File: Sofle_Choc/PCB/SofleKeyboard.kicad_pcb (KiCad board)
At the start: 2 copper layers, 143.4 x 111.8 mm, 84 parts, among them J2 4PIN, J3 OLED, P1 i2c_pin, P2 i2c_pin, SW1 SW_PUSH_LED, SW10 SW_PUSH_LED, SW11 SW_PUSH_LED, SW12 SW_PUSH_LED, SW13 SW_PUSH_LED, SW14 SW_PUSH_LED, SW15 SW_PUSH_LED, SW16 SW_PUSH_LED, SW17 SW_PUSH_LED, SW18 SW_PUSH_LED, SW19 SW_PUSH_LED, SW2 SW_PUSH_LED, SW20 SW_PUSH_LED, SW21 SW_PUSH_LED, SW22 SW_PUSH_LED, SW23 SW_PUSH_LED, SW24 SW_PUSH_LED, SW25 Rotary_Encoder_Switch, SW26 SW_PUSH_LED, SW27 SW_PUSH_LED, SW28 SW_PUSH_LED, SW29 SW_PUSH_LED, SW3 SW_PUSH_LED, SW30 SW_PUSH_LED, SW4 SW_PUSH_LED, SW5 SW_PUSH_LED, SW6 SW_PUSH_LED, SW7 SW_PUSH_LED, SW8 SW_PUSH_LED, SW9 SW_PUSH_LED, U1 ProMicro

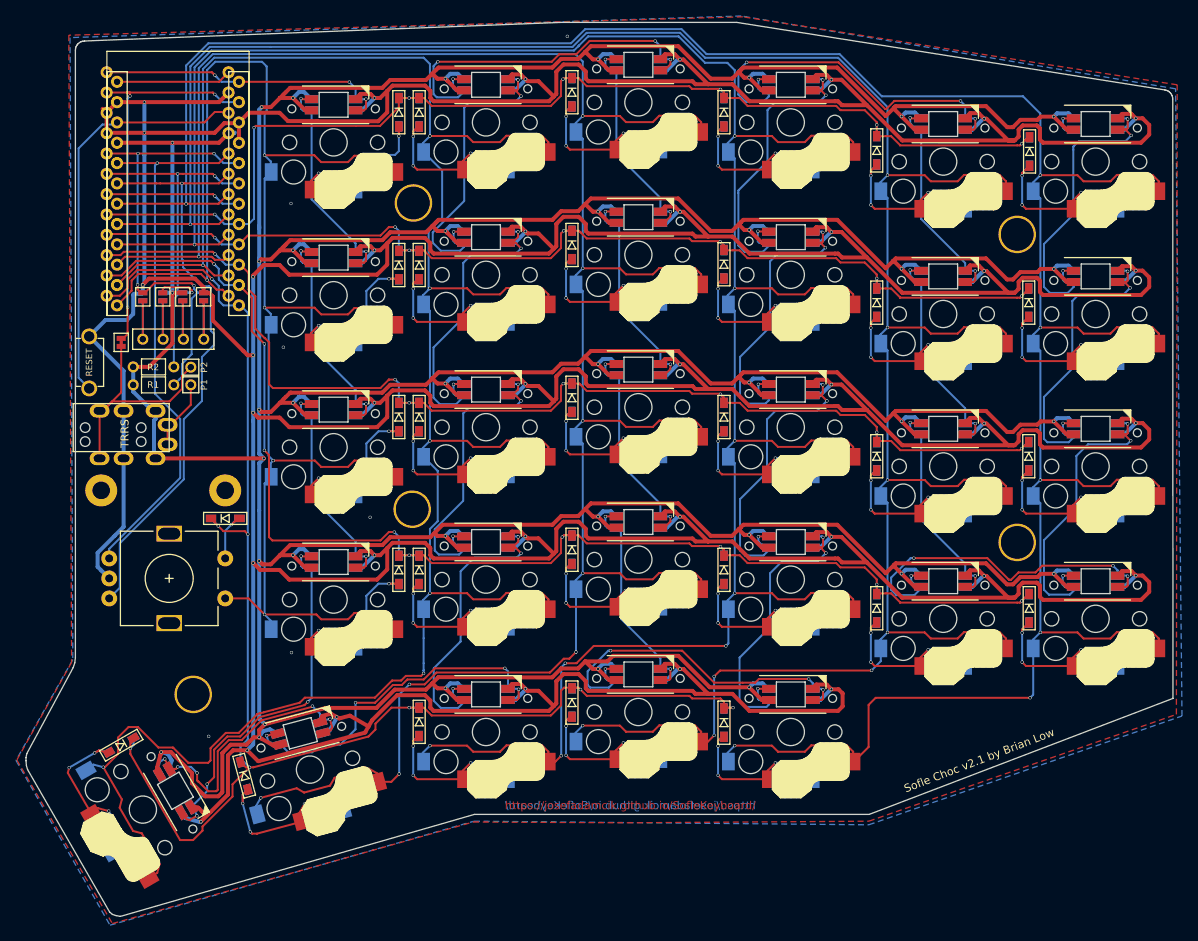
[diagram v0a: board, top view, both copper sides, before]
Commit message: First pass at comparison graphics Revised all keyboards to use outline stubbs Generated nested SVG's and color pallete
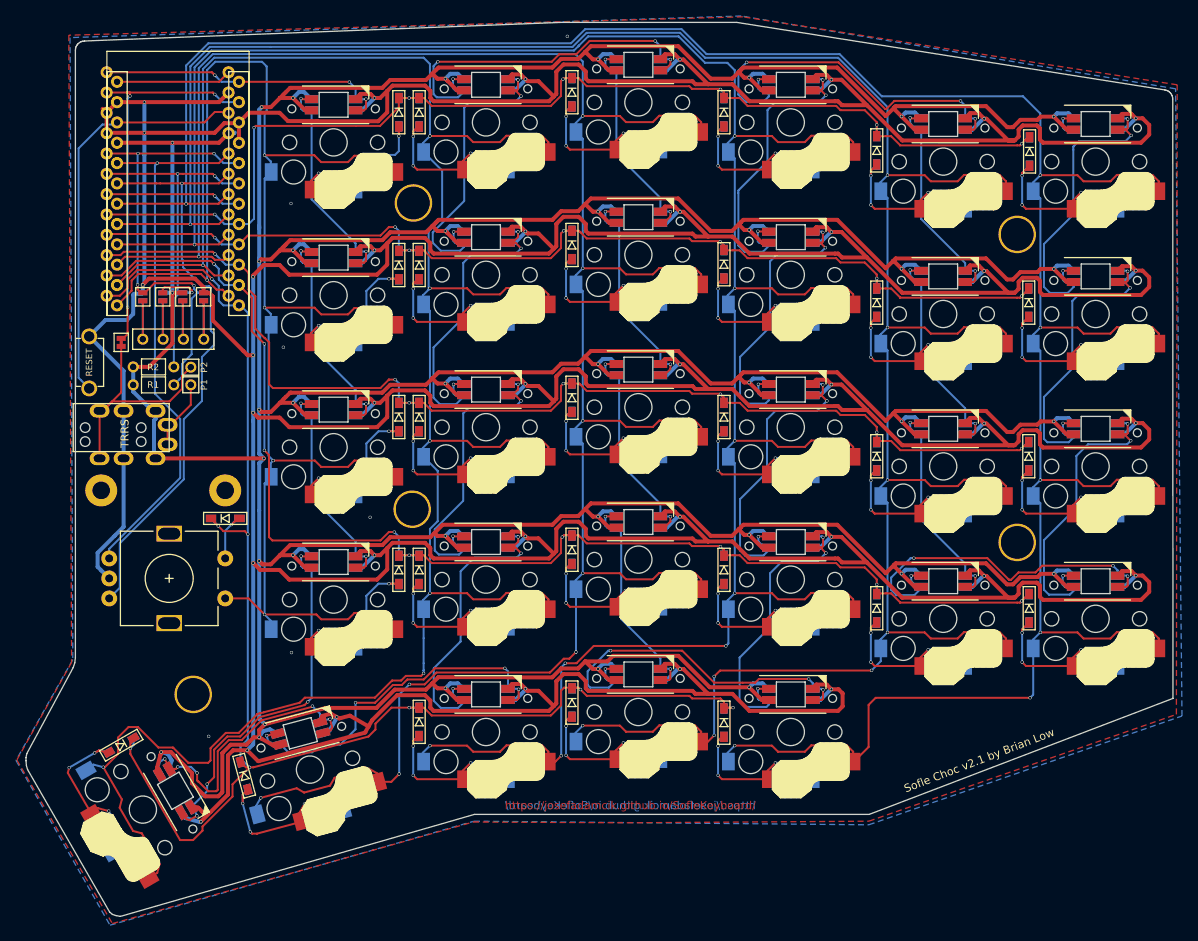
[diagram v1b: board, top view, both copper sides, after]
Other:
- net class Default removed
- net class GND removed
- net class VCC removed
